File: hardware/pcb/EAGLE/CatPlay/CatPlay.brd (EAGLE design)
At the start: 44 x 24 mm, 7 parts, among them Q1 2N7002

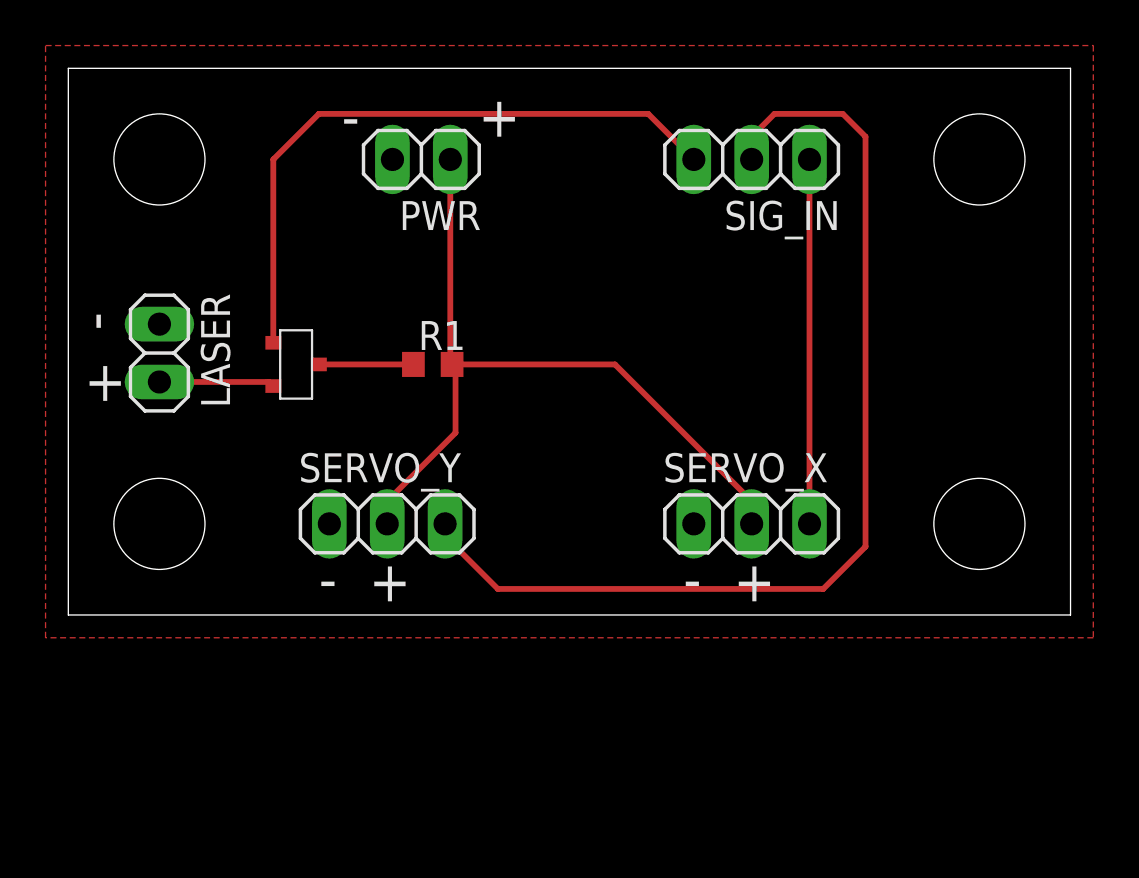
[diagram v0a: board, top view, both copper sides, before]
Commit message: Updated Schematic [CAT-4]
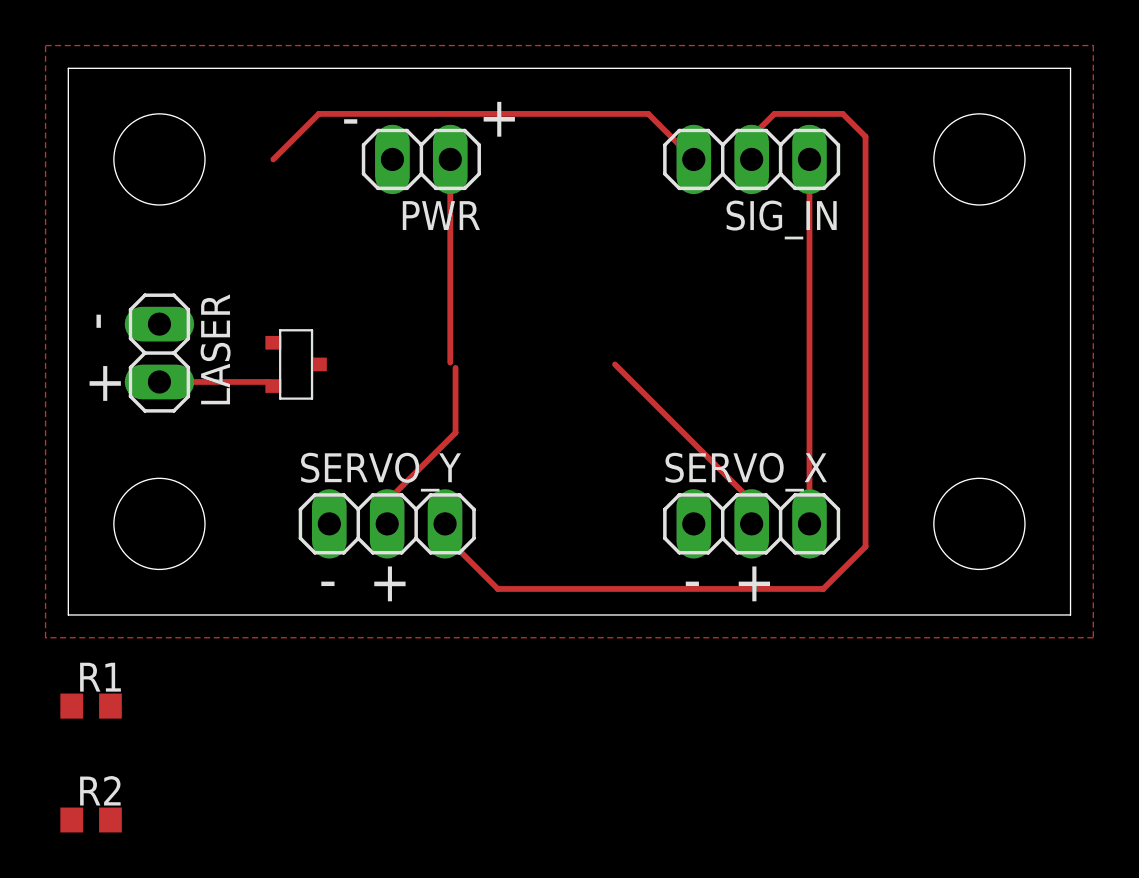
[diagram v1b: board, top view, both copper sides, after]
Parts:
- added R2: (no value), rcl:R0603
- R1: value (none) -> 1K
- moved R1 21.2 mm to (1.00, -4.00)
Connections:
- removed net L+: LASER.2, Q1.2
- removed net N$1: Q1.3, R1.1
- new net L-: LASER.1, R2.2
- new net N$3: Q1.3, R2.1
- net 5V: now also LASER.2; no longer R1.2
- net GND: now also Q1.2, R1.1; no longer LASER.1
- net LSR: now also R1.2
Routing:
- net LSR: track 28.2 -> 20.1 mm
- net L+: track 5.07 -> 0.00 mm
- net N$1: track 4.15 -> 0.00 mm
- net 5V: track 34.0 -> 31.3 mm
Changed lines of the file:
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@@
 </element>
 <element name="Q1" library="CatPlay" package="SOT-23" value="2N7002" x="10" y="11" smashed="yes" rot="R90"/>
-<element name="R1" library="rcl" library_urn="urn:adsk.eagle:library:334" package="R0603" package3d_urn="urn:adsk.eagle:package:23555/3" value="" x="16" y="11" smashed="yes">
-<attribute name="NAME" x="15.365" y="11.635" size="1.27" layer="25"/>
-<attribute name="POPULARITY" value="77" x="31.24" y="-15.67" size="1.778" layer="27" display="off"/>
-<attribute name="SPICEPREFIX" value="R" x="31.24" y="-15.67" size="1.778" layer="27" display="off"/>
-<attribute name="VALUE" x="15.365" y="9.095" size="1.27" layer="27"/>
-</element>
 <element name="SERVO_X" library="pinhead" library_urn="urn:adsk.eagle:library:325" package="1X03" package3d_urn="urn:adsk.eagle:package:22458/2" value="" x="30" y="4" smashed="yes">
 <attribute name="NAME" x="26.1138" y="5.8288" size="1.27" layer="25" ratio="10"/>
@@
 <attribute name="VALUE" x="33.81" y="23.175" size="1.27" layer="27" rot="R180"/>
 </element>
+<element name="R1" library="rcl" library_urn="urn:adsk.eagle:library:334" package="R0603" package3d_urn="urn:adsk.eagle:package:23555/3" value="1K" x="1" y="-4" smashed="yes">
+<attribute name="NAME" x="0.365" y="-3.365" size="1.27" layer="25"/>
+<attribute name="POPULARITY" value="77" x="1" y="-4" size="1.778" layer="27" display="off"/>
+<attribute name="SPICEPREFIX" value="R" x="1" y="-4" size="1.778" layer="27" display="off"/>
+<attribute name="VALUE" x="0.365" y="-5.905" size="1.27" layer="27"/>
+</element>
+<element name="R2" library="rcl" library_urn="urn:adsk.eagle:library:334" package="R0603" package3d_urn="urn:adsk.eagle:package:23555/3" value="" x="1" y="-9" smashed="yes">
+<attribute name="NAME" x="0.365" y="-8.365" size="1.27" layer="25"/>
+<attribute name="POPULARITY" value="77" x="1" y="-9" size="1.778" layer="27" display="off"/>
+<attribute name="SPICEPREFIX" value="R" x="1" y="-9" size="1.778" layer="27" display="off"/>
+<attribute name="VALUE" x="0.365" y="-10.905" size="1.27" layer="27"/>
+</element>
 </elements>
 <signals>
@@
 <contactref element="SERVO_X" pad="1"/>
 <contactref element="SERVO_Y" pad="1"/>
-<contactref element="LASER" pad="1"/>
 <contactref element="PWR" pad="2"/>
 <polygon width="0.254" layer="1">
@@
 <vertex x="-1" y="-1"/>
 </polygon>
-</signal>
-<signal name="L+">
-<contactref element="LASER" pad="2"/>
 <contactref element="Q1" pad="2"/>
-<wire x1="4" y1="10.23" x2="8.82" y2="10.23" width="0.254" layer="1"/>
-<wire x1="8.82" y1="10.23" x2="9" y2="10.05" width="0.254" layer="1"/>
+<contactref element="R1" pad="1"/>
+<wire x1="9" y1="10.05" x2="14.23" y2="20" width="0" layer="19" extent="1-1"/>
+<wire x1="11.46" y1="4" x2="9" y2="10.05" width="0" layer="19" extent="1-1"/>
+<wire x1="0.15" y1="-4" x2="11.46" y2="4" width="0" layer="19" extent="1-1"/>
+<wire x1="27.46" y1="4" x2="11.46" y2="4" width="0" layer="19" extent="1-1"/>
 </signal>
 <signal name="5V">
@@
 <contactref element="SERVO_Y" pad="2"/>
 <contactref element="PWR" pad="1"/>
-<contactref element="R1" pad="2"/>
-<wire x1="16.85" y1="11" x2="16.77" y2="11.08" width="0.254" layer="1"/>
 <wire x1="16.77" y1="11.08" x2="16.77" y2="20" width="0.254" layer="1"/>
 <wire x1="14" y1="4" x2="14" y2="5" width="0.254" layer="1"/>
 <wire x1="14" y1="5" x2="17" y2="8" width="0.254" layer="1"/>
 <wire x1="17" y1="8" x2="17" y2="10.85" width="0.254" layer="1"/>
-<wire x1="17" y1="10.85" x2="16.85" y2="11" width="0.254" layer="1"/>
 <wire x1="30" y1="4" x2="30" y2="5" width="0.254" layer="1"/>
 <wire x1="30" y1="5" x2="24" y2="11" width="0.254" layer="1"/>
-<wire x1="24" y1="11" x2="16.85" y2="11" width="0.254" layer="1"/>
+<contactref element="LASER" pad="2"/>
+<wire x1="4" y1="10.23" x2="8.82" y2="10.23" width="0.254" layer="1"/>
+<wire x1="17" y1="10.85" x2="24" y2="11" width="0" layer="19" extent="1-1"/>
+<wire x1="16.77" y1="11.08" x2="17" y2="10.85" width="0" layer="19" extent="1-1"/>
+<wire x1="8.82" y1="10.23" x2="14" y2="5" width="0" layer="19" extent="1-1"/>
 </signal>
 <signal name="SRV_X">
@@
 <signal name="LSR">
 <contactref element="SIG_IN" pad="3"/>
-<contactref element="Q1" pad="1"/>
 <wire x1="27.46" y1="20" x2="25.46" y2="22" width="0.254" layer="1"/>
 <wire x1="25.46" y1="22" x2="11" y2="22" width="0.254" layer="1"/>
 <wire x1="11" y1="22" x2="9" y2="20" width="0.254" layer="1"/>
-<wire x1="9" y1="20" x2="9" y2="11.95" width="0.254" layer="1"/>
+<contactref element="Q1" pad="1"/>
+<contactref element="R1" pad="2"/>
+<wire x1="9" y1="11.95" x2="9" y2="20" width="0" layer="19" extent="1-1"/>
+<wire x1="1.85" y1="-4" x2="9" y2="11.95" width="0" layer="19" extent="1-1"/>
 </signal>
-<signal name="N$1">
+<signal name="N$3">
 <contactref element="Q1" pad="3"/>
-<contactref element="R1" pad="1"/>
-<wire x1="11" y1="11" x2="15.15" y2="11" width="0.254" layer="1"/>
+<contactref element="R2" pad="1"/>
+<wire x1="0.15" y1="-9" x2="11" y2="11" width="0" layer="19" extent="1-1"/>
+</signal>
+<signal name="L-">
+<contactref element="R2" pad="2"/>
+<contactref element="LASER" pad="1"/>
+<wire x1="1.85" y1="-9" x2="4" y2="12.77" width="0" layer="19" extent="1-1"/>
 </signal>
 </signals>
